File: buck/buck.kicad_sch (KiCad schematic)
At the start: 15 parts, among them IC1 TPS630702RNMR

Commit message: made prod, gave components for everything
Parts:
- C1, C3: footprint Capacitor_SMD:C_0402_1005Metric_Pad0.74x0.62mm_HandSolder -> Capacitor_SMD:C_0805_2012Metric_Pad1.18x1.45mm_HandSolder
- renumbered gnd_out to gnd_out1, pwr_out to pwr_out1

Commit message: made prod with through hole mounts
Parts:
- EN1, gnd1, gnd_out1, pwr1, pwr_out1: footprint TestPoint:TestPoint_Pad_1.0x1.0mm -> TestPoint:TestPoint_THTPad_1.0x1.0mm_Drill0.5mm
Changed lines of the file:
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@@
 			)
 		)
-		(property "Footprint" "TestPoint:TestPoint_Pad_1.0x1.0mm"
+		(property "Footprint" "TestPoint:TestPoint_THTPad_1.0x1.0mm_Drill0.5mm"
 			(at 265.43 109.22 0)
 			(effects
@@
 			)
 		)
-		(property "Footprint" "TestPoint:TestPoint_Pad_1.0x1.0mm"
+		(property "Footprint" "TestPoint:TestPoint_THTPad_1.0x1.0mm_Drill0.5mm"
 			(at 99.06 91.44 0)
 			(effects
@@
 			)
 		)
-		(property "Footprint" "TestPoint:TestPoint_Pad_1.0x1.0mm"
+		(property "Footprint" "TestPoint:TestPoint_THTPad_1.0x1.0mm_Drill0.5mm"
 			(at 78.74 73.66 0)
 			(effects
@@
 			)
 		)
-		(property "Footprint" "TestPoint:TestPoint_Pad_1.0x1.0mm"
+		(property "Footprint" "TestPoint:TestPoint_THTPad_1.0x1.0mm_Drill0.5mm"
 			(at 265.43 80.01 0)
 			(effects
@@
 			)
 		)
-		(property "Footprint" "TestPoint:TestPoint_Pad_1.0x1.0mm"
+		(property "Footprint" "TestPoint:TestPoint_THTPad_1.0x1.0mm_Drill0.5mm"
 			(at 78.74 99.06 0)
 			(effects

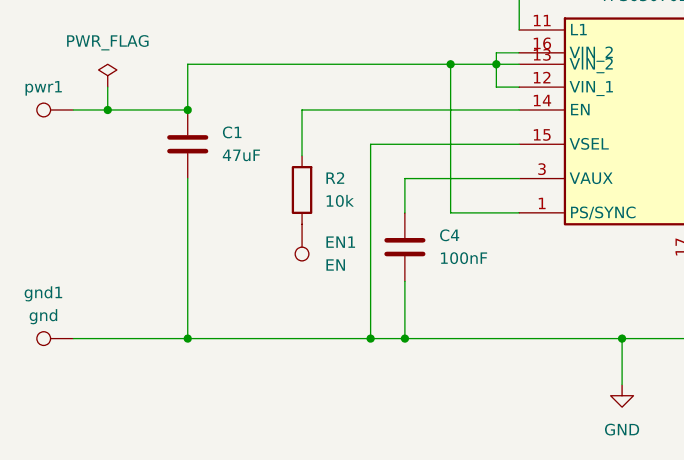
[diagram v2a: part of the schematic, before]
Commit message: redesigned with new en tie to gnd and 4x pads
added name under IC and near back of board
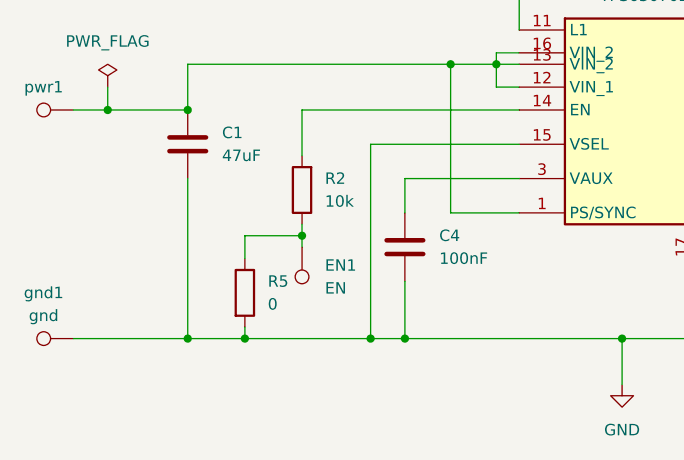
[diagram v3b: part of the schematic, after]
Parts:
- added R5: 0, Resistor_SMD:R_0402_1005Metric_Pad0.72x0.64mm_HandSolder, symbol Device:R
- EN1, gnd1, gnd_out1, pwr1, pwr_out1: footprint TestPoint:TestPoint_THTPad_1.0x1.0mm_Drill0.5mm -> TestPoint:TestPoint_Loop_D3.80mm_Drill2.5mm
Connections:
- net GND: now also R5.2
- net at EN1.1, R2.1: now also R5.1
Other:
- moved on the sheet: EN1
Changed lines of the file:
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@@
+	)
+	(junction
+		(at 104.14 92.71)
+		(diameter 0)
+		(color 0 0 0 0)
 	)
 	(junction
@@
 		(color 0 0 0 0)
 	)
+	(junction
+		(at 97.79 104.14)
+		(diameter 0)
+		(color 0 0 0 0)
+	)
 	(wire
 		(pts
@@
 	(wire
 		(pts
+			(xy 97.79 104.14) (xy 111.76 104.14)
+		)
+		(stroke
+			(width 0)
+			(type default)
+		)
+	)
+	(wire
+		(pts
 			(xy 165.1 77.47) (xy 165.1 104.14)
 		)
@@
 	(wire
 		(pts
-			(xy 91.44 104.14) (xy 111.76 104.14)
+			(xy 97.79 102.87) (xy 97.79 104.14)
+		)
+		(stroke
+			(width 0)
+			(type default)
+		)
+	)
+	(wire
+		(pts
+			(xy 91.44 104.14) (xy 97.79 104.14)
 		)
 		(stroke
@@
 	(wire
 		(pts
+			(xy 97.79 92.71) (xy 97.79 95.25)
+		)
+		(stroke
+			(width 0)
+			(type default)
+		)
+	)
+	(wire
+		(pts
 			(xy 128.27 72.39) (xy 125.73 72.39)
 		)
@@
 	(wire
 		(pts
+			(xy 104.14 92.71) (xy 104.14 91.44)
+		)
+		(stroke
+			(width 0)
+			(type default)
+		)
+	)
+	(wire
+		(pts
+			(xy 104.14 93.98) (xy 104.14 92.71)
+		)
+		(stroke
+			(width 0)
+			(type default)
+		)
+	)
+	(wire
+		(pts
 			(xy 181.61 85.09) (xy 181.61 83.82)
 		)
@@
 		(pts
 			(xy 115.57 104.14) (xy 139.7 104.14)
+		)
+		(stroke
+			(width 0)
+			(type default)
+		)
+	)
+	(wire
+		(pts
+			(xy 97.79 92.71) (xy 104.14 92.71)
 		)
 		(stroke
@@
 			)
 		)
-		(property "Footprint" "TestPoint:TestPoint_THTPad_1.0x1.0mm_Drill0.5mm"
+		(property "Footprint" "TestPoint:TestPoint_Loop_D3.80mm_Drill2.5mm"
 			(at 265.43 109.22 0)
 			(effects
@@
 	(symbol
 		(lib_id "Connector:TestPoint")
-		(at 104.14 91.44 180)
+		(at 104.14 93.98 180)
 		(unit 1)
 		(exclude_from_sim no)
@@
 		(fields_autoplaced yes)
 		(property "Reference" "EN1"
-			(at 106.68 93.4719 0)
+			(at 106.68 96.0119 0)
 			(effects
 				(font
@@
 		)
 		(property "Value" "EN"
-			(at 106.68 96.0119 0)
+			(at 106.68 98.5519 0)
 			(effects
 				(font
@@
 			)
 		)
-		(property "Footprint" "TestPoint:TestPoint_THTPad_1.0x1.0mm_Drill0.5mm"
-			(at 99.06 91.44 0)
+		(property "Footprint" "TestPoint:TestPoint_Loop_D3.80mm_Drill2.5mm"
+			(at 99.06 93.98 0)
 			(effects
 				(font
@@
 		)
 		(property "Datasheet" "~"
-			(at 99.06 91.44 0)
+			(at 99.06 93.98 0)
 			(effects
 				(font
@@
 		)
 		(property "Description" "test point"
-			(at 104.14 91.44 0)
+			(at 104.14 93.98 0)
 			(effects
 				(font
@@
 			)
 		)
-		(property "Footprint" "TestPoint:TestPoint_THTPad_1.0x1.0mm_Drill0.5mm"
+		(property "Footprint" "TestPoint:TestPoint_Loop_D3.80mm_Drill2.5mm"
 			(at 78.74 73.66 0)
 			(effects
@@
 			)
 		)
-		(property "Footprint" "TestPoint:TestPoint_THTPad_1.0x1.0mm_Drill0.5mm"
+		(property "Footprint" "TestPoint:TestPoint_Loop_D3.80mm_Drill2.5mm"
 			(at 265.43 80.01 0)
 			(effects
@@
 			)
 		)
-		(property "Footprint" "TestPoint:TestPoint_THTPad_1.0x1.0mm_Drill0.5mm"
+		(property "Footprint" "TestPoint:TestPoint_Loop_D3.80mm_Drill2.5mm"
 			(at 78.74 99.06 0)
 			(effects
@@
 					(unit 1)
 				)
+			)
+		)
+	)
+	(symbol
+		(lib_id "Device:R")
+		(at 97.79 99.06 0)
+		(unit 1)
+		(exclude_from_sim no)
+		(in_bom yes)
+		(on_board yes)
+		(dnp no)
+		(fields_autoplaced yes)
+		(property "Reference" "R5"
+			(at 100.33 97.7899 0)
+			(effects
+				(font
+					(size 1.27 1.27)
+				)
+				(justify left)
+			)
+		)
+		(property "Value" "0"
+			(at 100.33 100.3299 0)
+			(effects
+				(font
+					(size 1.27 1.27)
+				)
+				(justify left)
+			)
+		)
+		(property "Footprint" "Resistor_SMD:R_0402_1005Metric_Pad0.72x0.64mm_HandSolder"
+			(at 96.012 99.06 90)
+			(effects
+				(font
+					(size 1.27 1.27)
+				)
+				(hide yes)
+			)
+		)
+		(property "Datasheet" "~"
+			(at 97.79 99.06 0)
+			(effects
+				(font
+					(size 1.27 1.27)
+				)
+				(hide yes)
+			)
+		)
+		(property "Description" "Resistor"
+			(at 97.79 99.06 0)
+			(effects
+				(font
+					(size 1.27 1.27)
+				)
+				(hide yes)
+			)
+		)
+		(pin "2"
+		)
+		(pin "1"
+		)
+		(instances
+			(project "buck"
+				(path "/09b05005-515b-4cb8-8c28-d9a88da80a5e"
+					(reference "R5")
+					(unit 1)
+				)
